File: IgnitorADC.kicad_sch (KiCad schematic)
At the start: 16 parts, among them U7 ADS112C04

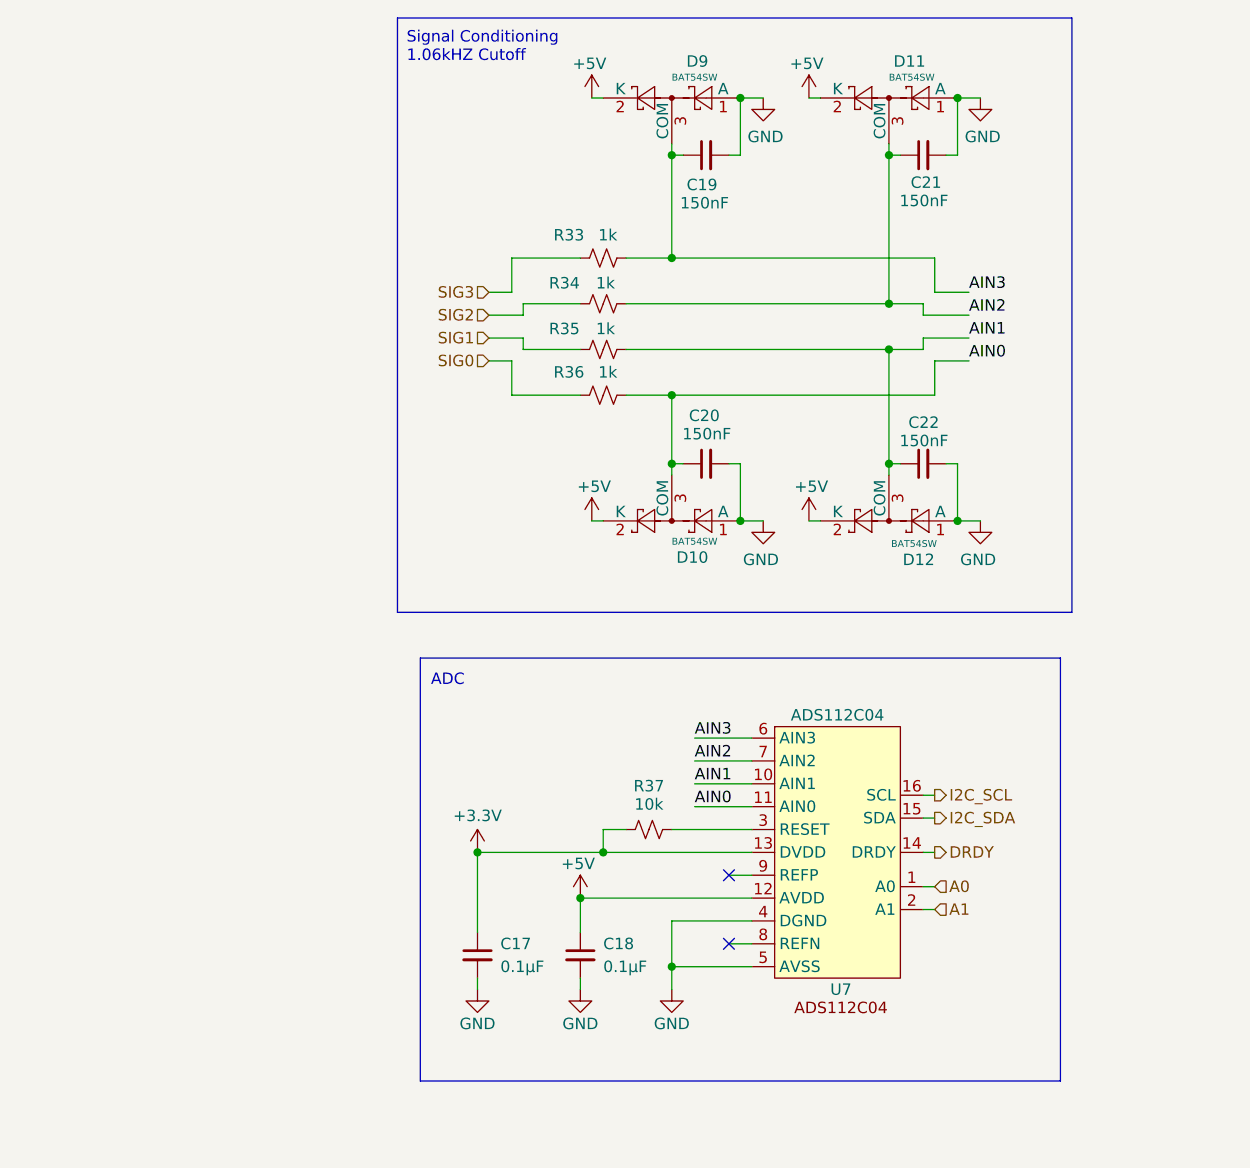
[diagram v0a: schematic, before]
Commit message: fix ignitor resistance read circuit to use correct PGA reference
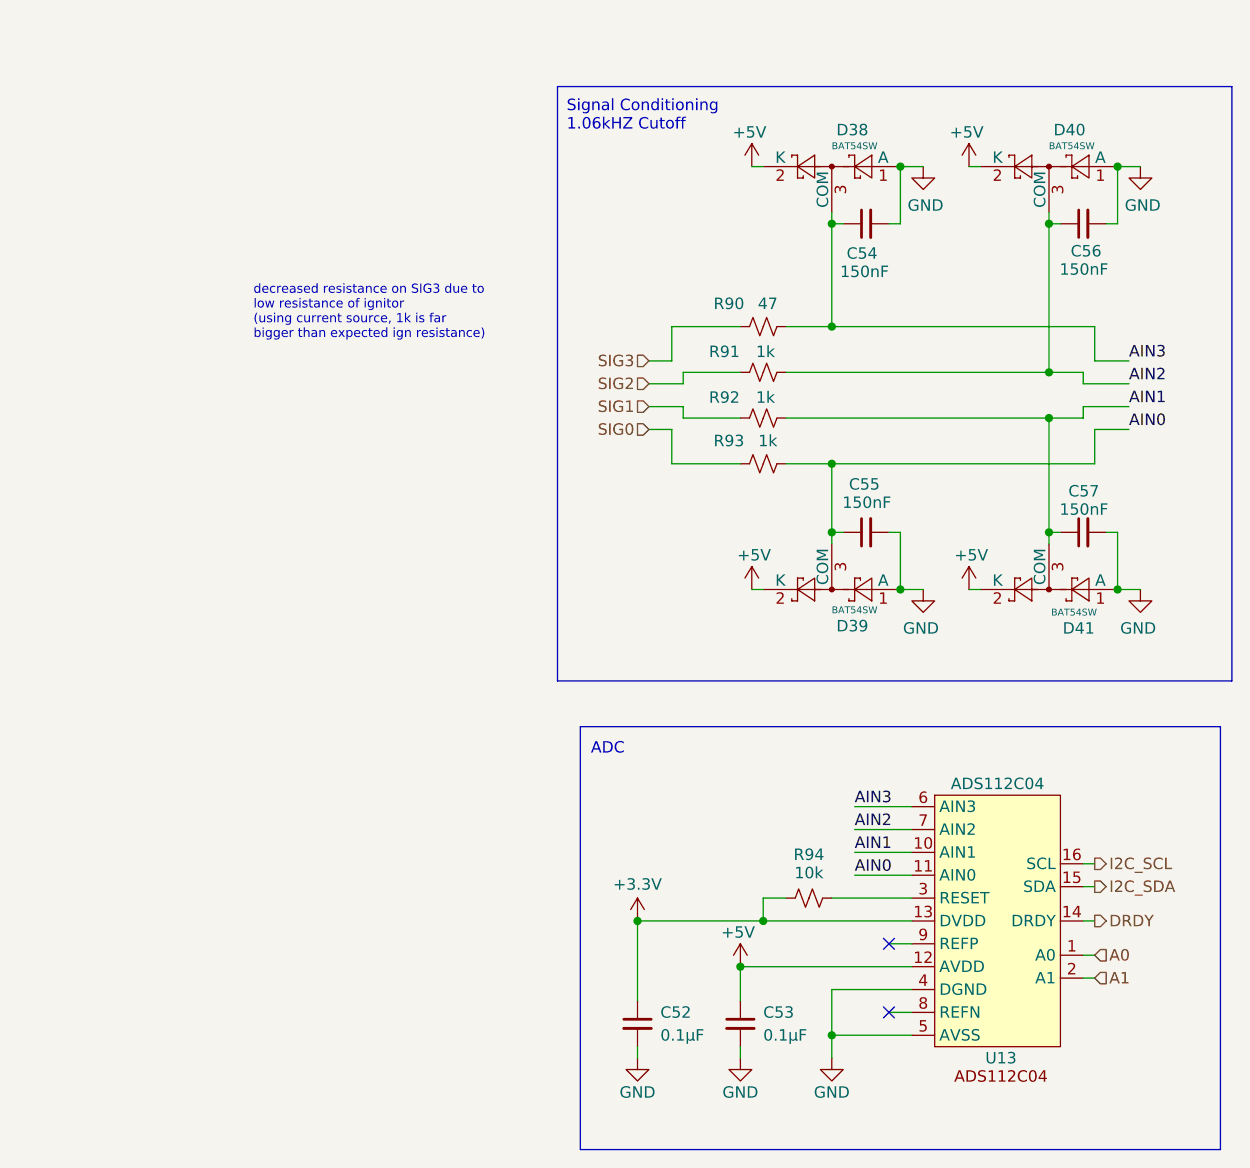
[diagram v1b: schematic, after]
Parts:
- removed C17, C18: 0.1μF, Capacitor_SMD:C_0402_1005Metric, symbol Device:C_Small
- removed C19, C20, C21, C22: 150nF, Capacitor_SMD:C_0805_2012Metric, symbol Device:C_Small
- removed D10, D11, D12, D9: BAT54SW, Package_TO_SOT_SMD:SOT-323_SC-70, symbol Diode:BAT54SW
- removed R33, R34, R35, R36: 1k, Resistor_SMD:R_0402_1005Metric, symbol Device:R_Small_US
- removed R37: 10k, Resistor_SMD:R_0402_1005Metric, symbol Device:R_Small_US
- removed U7: ADS112C04, Package_SO:TSSOP-16_4.4x5mm_P0.65mm, symbol ADS112C04:ADS112C04
- added C52, C53: 0.1μF, Capacitor_SMD:C_0402_1005Metric, symbol Device:C_Small
- added C54, C55, C56, C57: 150nF, Capacitor_SMD:C_0805_2012Metric, symbol Device:C_Small
- added D38, D39, D40, D41: BAT54SW, Package_TO_SOT_SMD:SOT-323_SC-70, symbol Diode:BAT54SW
- added R90: 47, Resistor_SMD:R_0402_1005Metric, symbol Device:R_Small_US
- added R91, R92, R93: 1k, Resistor_SMD:R_0402_1005Metric, symbol Device:R_Small_US
- added R94: 10k, Resistor_SMD:R_0402_1005Metric, symbol Device:R_Small_US
- added U13: ADS112C04, Package_SO:TSSOP-16_4.4x5mm_P0.65mm, symbol ADS112C04:ADS112C04
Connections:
- net +3.3V: now also C52.1, R94.1, U13.13 (DVDD)
- net +5V: now also C53.1, D38.2 (K), D39.2 (K), D40.2 (K), D41.2 (K), U13.12 (AVDD)
- net A0: now also U13.1 (A0)
- net A1: now also U13.2 (A1)
- net AIN0: now also C55.1, D39.3 (COM), R93.2, U13.11 (AIN0)
- net AIN1: now also C57.1, D41.3 (COM), R92.2, U13.10 (AIN1)
- net AIN2: now also C56.1, D40.3 (COM), R91.2, U13.7 (AIN2)
- net AIN3: now also C54.1, D38.3 (COM), R90.2, U13.6 (AIN3)
- net DRDY: now also U13.14 (DRDY)
- net GND: now also C52.2, C53.2, C54.2, C55.2, C56.2, C57.2, D38.1 (A), D39.1 (A), D40.1 (A), D41.1 (A), U13.4 (DGND), U13.5 (AVSS)
- net I2C_SCL: now also U13.16 (SCL)
- net I2C_SDA: now also U13.15 (SDA)
- net SIG0: now also R93.1
- net SIG1: now also R92.1
- net SIG2: now also R91.1
- net SIG3: now also R90.1
- new net: R94.2, U13.3 (RESET)
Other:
- note added: "decreased resistance on SIG3 due to low resistance of ignitor (using current source, 1k is far bigger than expected ign resistance)"
- company: Queen's Rocket Engineering Team -> (none)

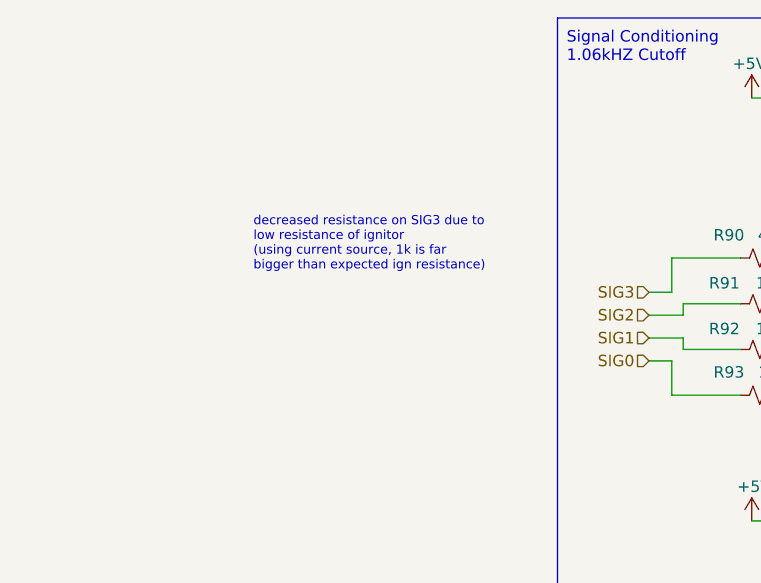
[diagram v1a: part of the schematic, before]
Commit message: add some comments to clarify ign_resist_read circuitry and implementation
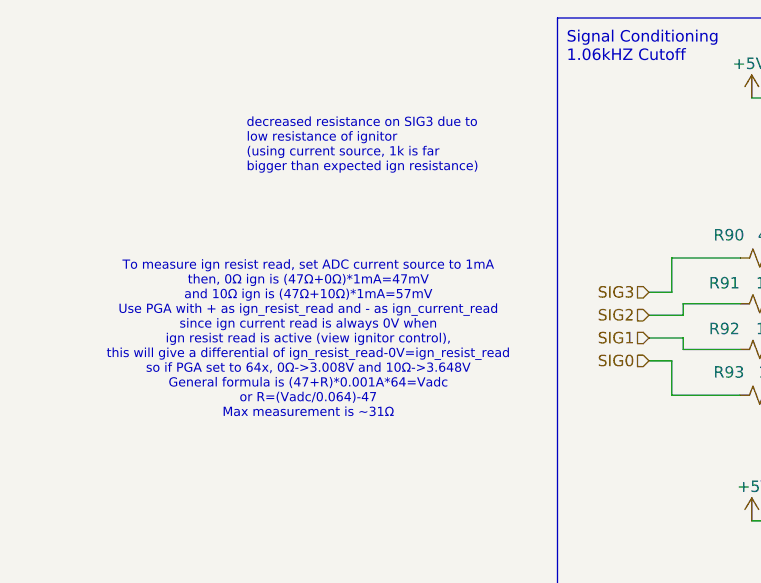
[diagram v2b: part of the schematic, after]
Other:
- note added: "To measure ign resist read, set ADC current source to 1mA then, 0Ω ign is (47Ω+0Ω)*1mA=47mV and 10Ω ign is (47Ω+10Ω)*1mA=57mV Use PGA with + as ign_resist_read and - as ign_current_read since ign current read is always 0V when ign resist read is active (view ignitor control), this will give a differential of ign_resist_read-0V=ign_resist_read so if PGA set to 64x, 0Ω->3.008V and 10Ω->3.648V Gener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"
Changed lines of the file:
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@@
+		)
+	)
+	(text "To measure ign resist read, set ADC current source to 1mA\nthen, 0Ω ign is (47Ω+0Ω)*1mA=47mV\nand 10Ω ign is (47Ω+10Ω)*1mA=57mV\nUse PGA with + as ign_resist_read and - as ign_current_read\nsince ign current read is always 0V when\nign resist read is active (view ignitor control),\nthis will give a differential of ign_resist_read-0V=ign_resist_read\nso if PGA set to 64x, 0Ω->3.008V and 10Ω->3.648V\nGeneral formula is (47+R)*0.001A*64=Vadc\nor R=(Vadc/0.064)-47\nMax measurement is ~31Ω"
+		(exclude_from_sim no)
+		(at 72.644 71.374 0)
+		(effects
+			(font
+				(size 1.016 1.016)
+				(thickness 0.127)
+			)
 		)
 	)
@@
 	(text "decreased resistance on SIG3 due to\nlow resistance of ignitor\n(using current source, 1k is far\nbigger than expected ign resistance)"
 		(exclude_from_sim no)
-		(at 66.548 60.706 0)
+		(at 65.786 49.784 0)
 		(effects
 			(font

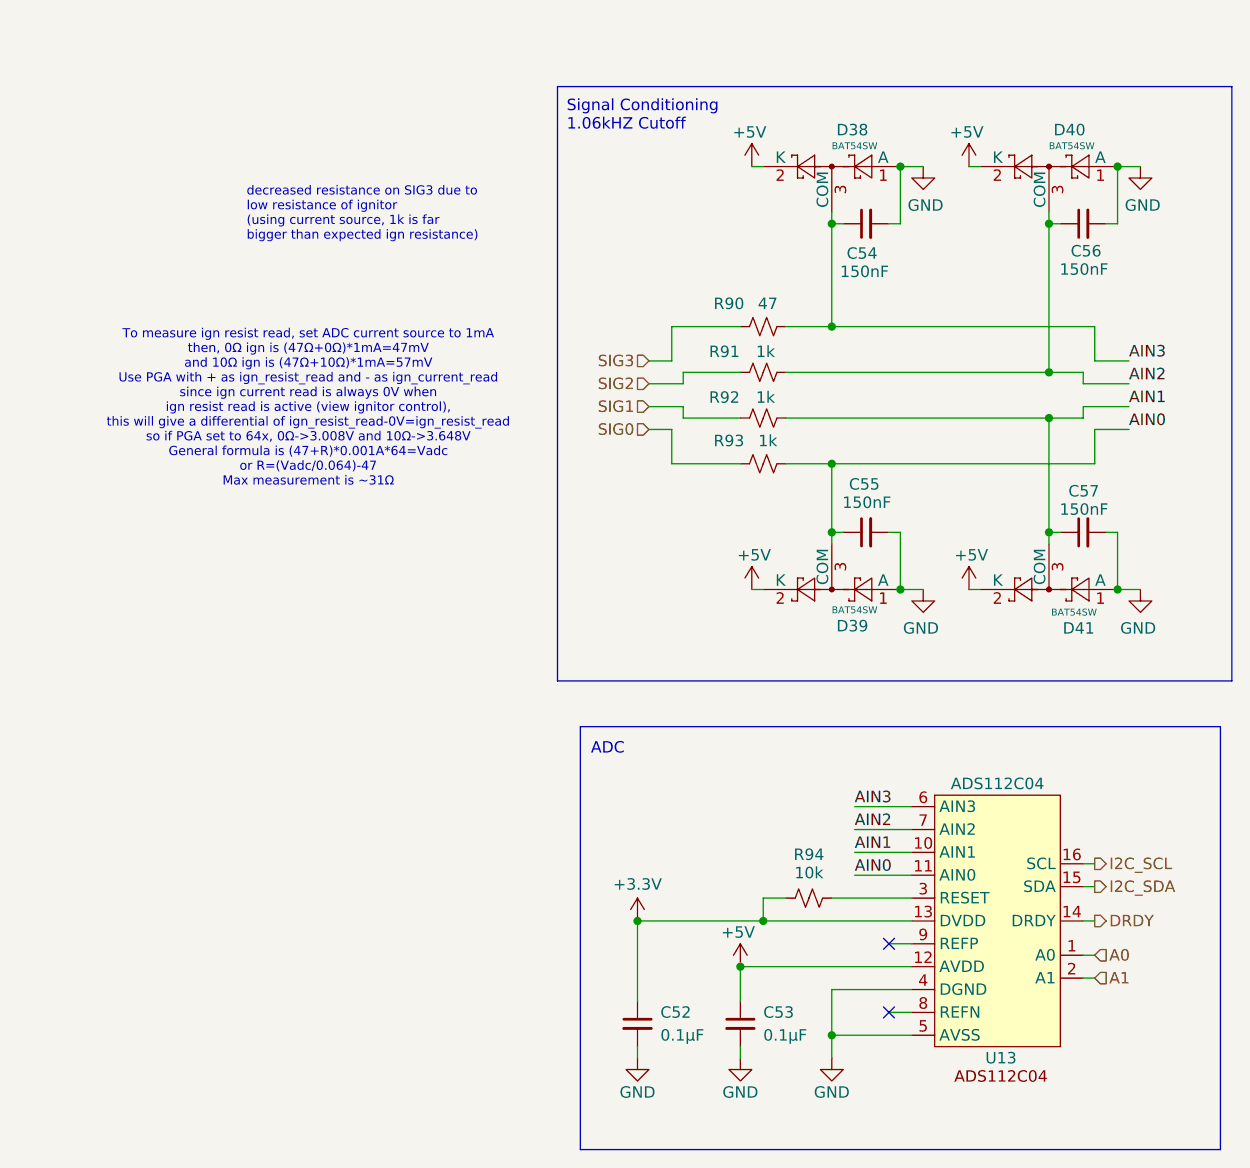
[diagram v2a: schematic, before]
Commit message: add capacitor and resistor footprints
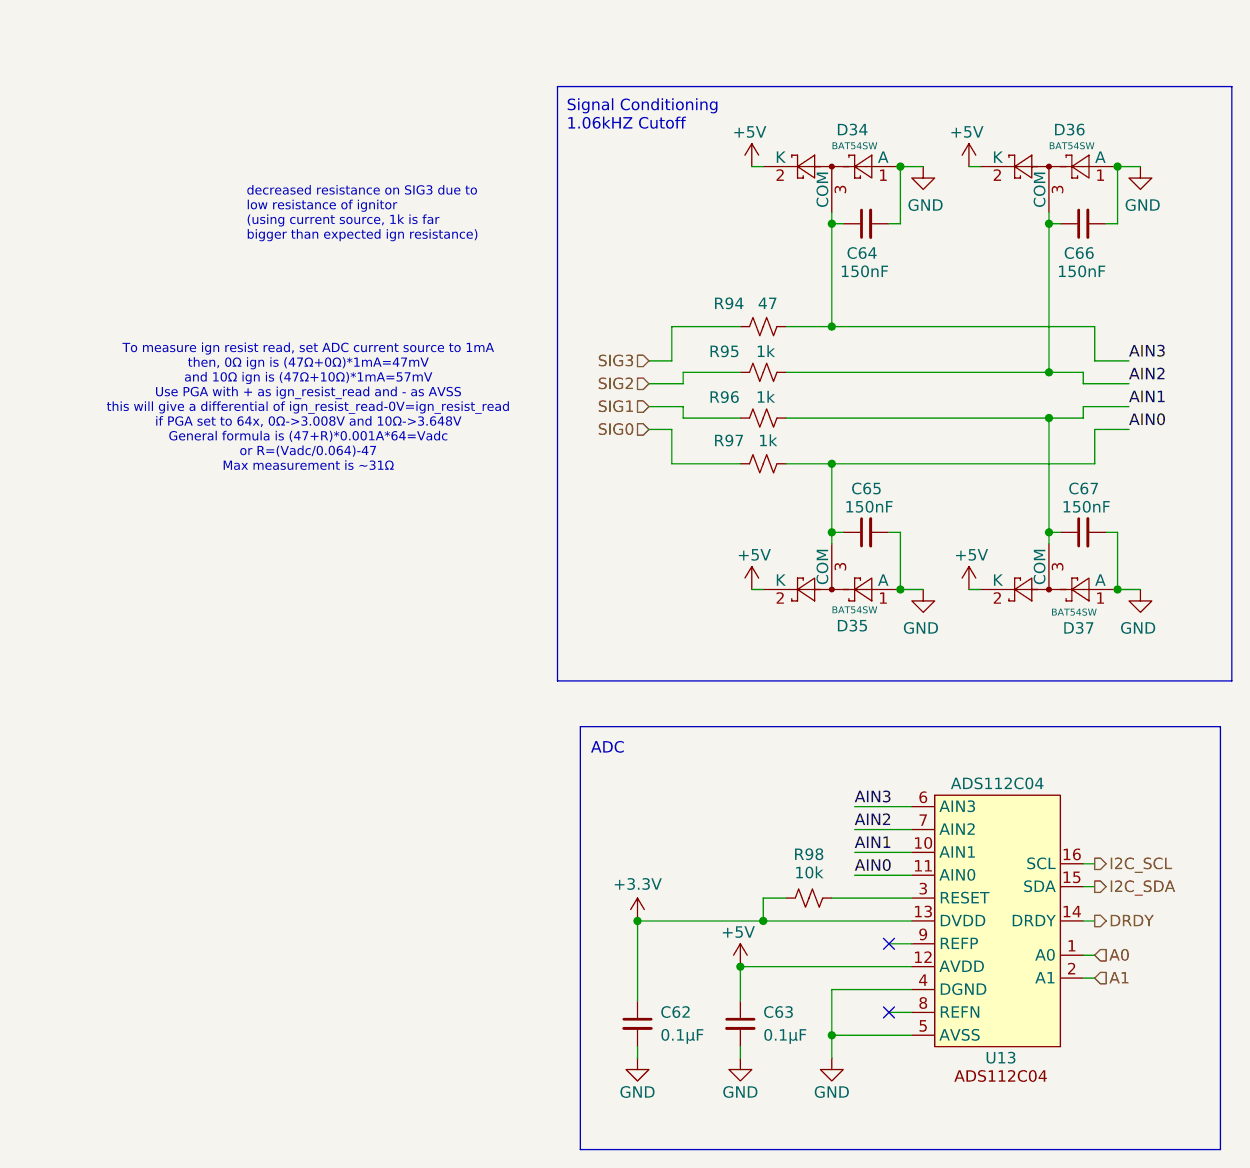
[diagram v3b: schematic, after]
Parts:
- removed C54, C55, C56, C57: 150nF, Capacitor_SMD:C_0805_2012Metric, symbol Device:C_Small
- added C64, C65, C66, C67: 150nF, Capacitor_SMD:C_0402_1005Metric, symbol Device:C_Small
- C62: renamed from C52; LCSC C1525 -> C307331
- C63: renamed from C53; LCSC C1525 -> C307331
- D34: renamed from D38; LCSC (none) -> C83575
- D35: renamed from D39; LCSC (none) -> C83575
- D36: renamed from D40; LCSC (none) -> C83575
- D37: renamed from D41; LCSC (none) -> C83575
- U13: ADC Number 1 -> (none); I2C Address 100 0000 -> (none)
- renumbered R90 to R94, R91 to R95, R92 to R96, R93 to R97, R94 to R98
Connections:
- net AIN0: now also C65.1
- net AIN1: now also C67.1
- net AIN2: now also C66.1
- net AIN3: now also C64.1
- net GND: now also C64.2, C65.2, C66.2, C67.2
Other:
- note added: "To measure ign resist read, set ADC current source to 1mA then, 0Ω ign is (47Ω+0Ω)*1mA=47mV and 10Ω ign is (47Ω+10Ω)*1mA=57mV Use PGA with + as ign_resist_read and - as AVSS this will give a differential of ign_resist_read-0V=ign_resist_read if PGA set to 64x, 0Ω->3.008V and 10Ω->3.648V General formula is (47+R)*0.001A*64=Vadc or R=(Vadc/0.064)-47 Max measurement is ~31Ω"
- note removed: "To measure ign resist read, set ADC current source to 1mA then, 0Ω ign is (47Ω+0Ω)*1mA=47mV and 10Ω ign is (47Ω+10Ω)*1mA=57mV Use PGA with + as ign_resist_read and - as ign_current_read since ign current read is always 0V when ign resist read is active (view ignitor control), this will give a differential of ign_resist_read-0V=ign_resist_read so if PGA set to 64x, 0Ω->3.008V and 10Ω->3.648V Gener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"

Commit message: change connectors and more progress on pcb
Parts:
- R94: LCSC (none) -> C445569
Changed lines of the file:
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@@
+			)
+		)
+		(property "LCSC" "C445569"
+			(at 123.19 62.23 90)
+			(effects
+				(font
+					(size 1.27 1.27)
+				)
+				(hide yes)
 			)
 		)
